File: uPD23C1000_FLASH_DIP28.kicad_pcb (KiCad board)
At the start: 2 copper layers, 16.4 x 34.2 mm, 7 parts, among them J1 uPD23C1000, J2 Conn_1x2, J3 Conn_1x3, U1 GLS29EE010 (TSOP), U2 SST39SF010 (TSOP), U3 SST39SF010 / GLS29EE010 (PLCC)

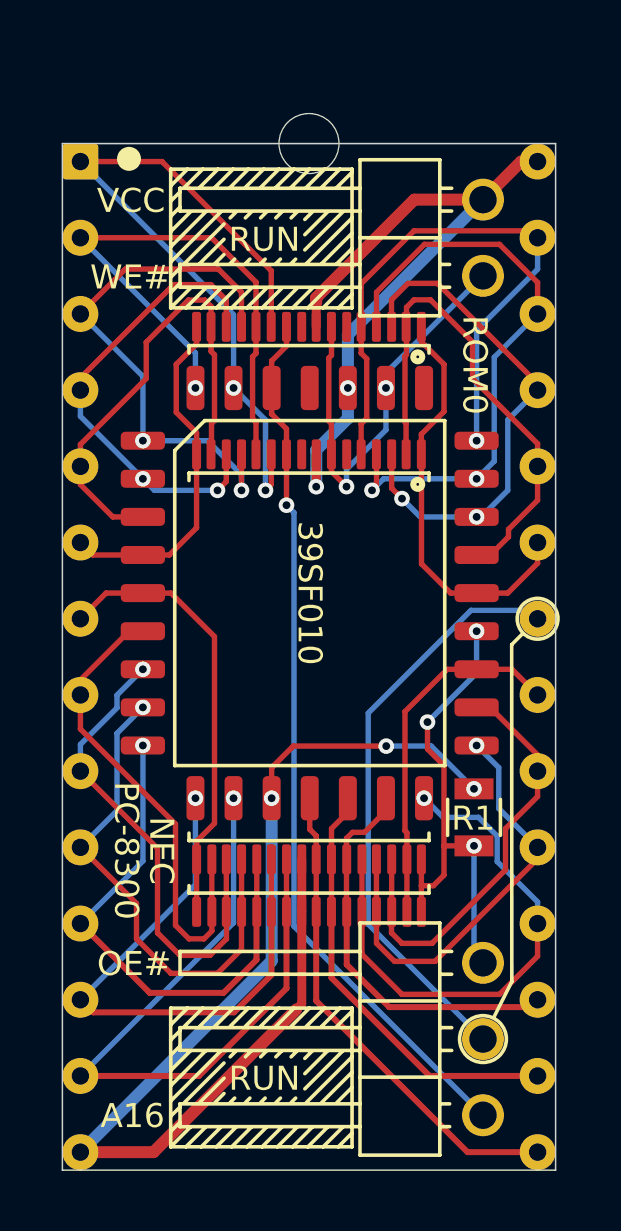
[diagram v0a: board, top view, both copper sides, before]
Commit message: FlashROM_8300: tsop footprints, zone fills
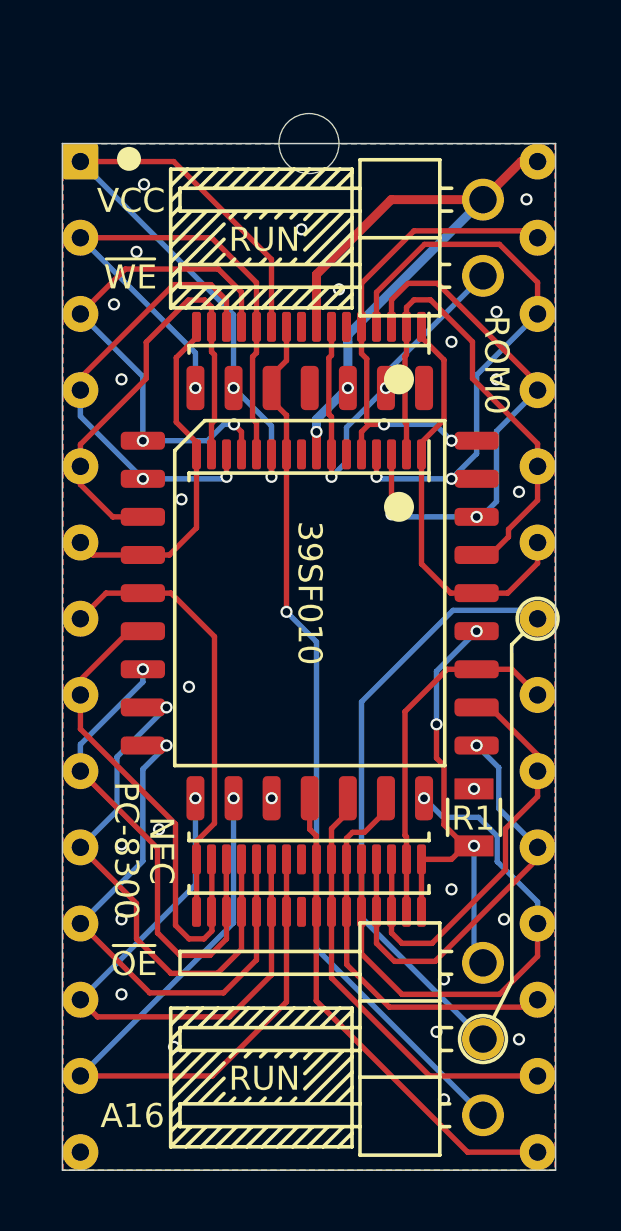
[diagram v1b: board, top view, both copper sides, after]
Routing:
- net /GND: track 37.3 -> 0.00 mm, vias 3 -> 26
- net /A14: track 20.2 -> 16.4 mm, vias 1 -> 2
- net /VCC: track 23.2 -> 21.5 mm
- net /A7: track 18.1 -> 16.8 mm
- net /D0: track 17.4 -> 18.5 mm
- net /A0: track 16.7 -> 17.8 mm
- net /~OE: track 16.7 -> 15.8 mm
- net /A15: track 24.5 -> 23.9 mm
- net /~WE: track 14.5 -> 13.9 mm
- net /A16_OE: track 19.6 -> 20.2 mm
- net /A8: track 17.1 -> 17.6 mm
- added copper zone on B.Cu, net /GND
- added copper zone on F.Cu, net /GND
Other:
- net class Default: clearance 0.2 -> 0.1524; trace_width 0.25 -> 0.18; via_dia 0.8 -> 0.4064; via_drill 0.4 -> 0.254
- rule trace_clearance: 0.2 -> 0.1524
- rule trace_min: 0.16 -> 0.1524
- rule via_min_drill: 0.26 -> 0.254
- rule via_min_size: 0.52 -> 0.4064
- board text added: "Connect ~WE~ to programmer pin 31"
- board text added: "Move A16 jumper to ~OE~"
- board text added: "Remove VCC/~WE~ jumper"
- board text added: "~OE"
- board text added: "~WE"
- board text removed: "Connect WE# to programmer pin 31"
- board text removed: "Move A16 jumper to OE#"
- board text removed: "OE#"
- board text removed: "Remove VCC/WE# jumper"
- board text removed: "WE#"

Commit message: minor tidying
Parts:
- moved J2 1.89 mm to (155.7, 85.4)
- moved U1 1.30 mm to (150.0, 97.5)
- moved J1 1.25 mm to (150.0, 98.8)
- moved J3 0.66 mm to (155.7, 114.6)
- moved R1 0.60 mm to (155.4, 106.0)
- moved U2 0.45 mm to (150.0, 100.5)
- moved U3 0.42 mm to (150.0, 97.5)
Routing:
- net /GND: track 0.00 -> 24.4 mm, vias 26 -> 2
- net /A15: track 23.9 -> 17.1 mm, vias 2 -> 0
- net /D6: track 17.8 -> 11.2 mm, vias 1 -> 2
- net /A14: track 16.4 -> 22.3 mm, vias 2 -> 1
- net /A16_OE: track 20.2 -> 15.4 mm
- net /VCC: track 21.5 -> 17.4 mm, vias 2 -> 0
- net /~CE: track 14.4 -> 10.4 mm
- net /~WE: track 13.9 -> 16.8 mm, vias 2 -> 3
- net /D0: track 18.5 -> 15.7 mm
- net /A0: track 17.8 -> 15.0 mm
- net /D7: track 14.5 -> 11.8 mm, vias 1 -> 0
- net /A12: track 18.8 -> 16.3 mm, vias 1 -> 3
- net /~OE: track 15.8 -> 13.3 mm, vias 3 -> 2
- net /D2: track 24.0 -> 21.6 mm
- net /A16: track 29.4 -> 31.6 mm
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- removed copper zone on B.Cu, net /GND
- removed copper zone on F.Cu, net /GND
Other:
- board size 16.4 x 34.2 mm -> 16.6 x 34.4 mm
- board text added: "29F010 39SF010 29EE010"
- board text added: "29F010 to uPD23C1000"
- board text added: "Move the A16 jumper to ~OE~"
- board text added: "Remove the VCC/~WE~ jumper"
- board text added: "Set programmer for installed chip (ex: SST39SF010 not uPD23C1000)"
- board text added: "github.com/bkw777/aDIPters"
- board text removed: "39SF010"
- board text removed: "Configure programmer for PLCC version of chip (even if chip is TSOP)"
- board text removed: "Move A16 jumper to ~OE~"
- board text removed: "NEC"
- board text removed: "NEC PC-8300 System ROM"
- board text removed: "PC-8300"
- board text removed: "ROM0"
- board text removed: "Remove VCC/~WE~ jumper"
- board text removed: "http://tandy.wiki/FlashROM_8300"

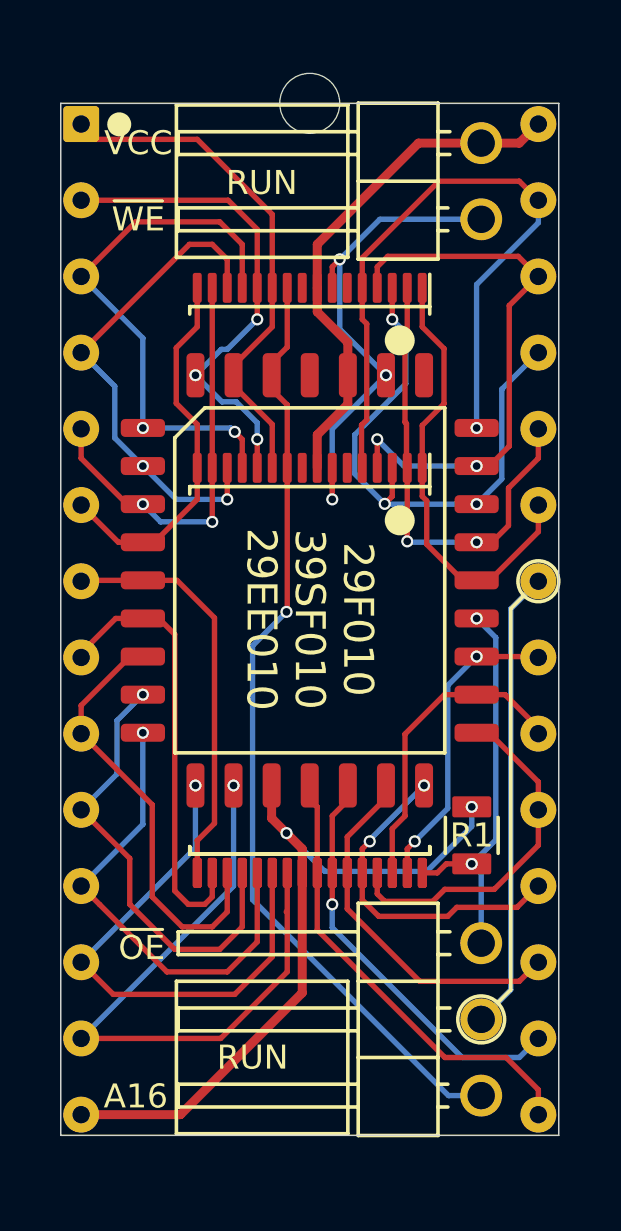
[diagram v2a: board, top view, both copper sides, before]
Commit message: upD23C1000 add A17 & R2
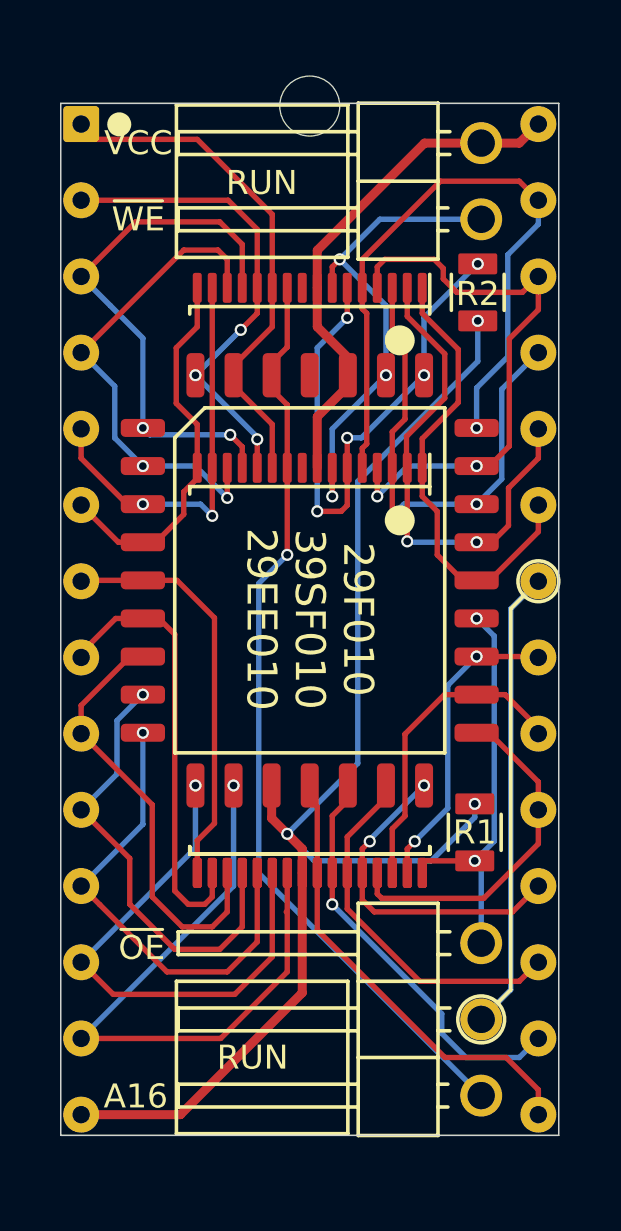
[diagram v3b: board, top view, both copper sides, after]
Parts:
- added R2: 47k, 000_LOCAL:R_0805, F.Cu at (155.6, 87.8)
- J1: footprint 000_LOCAL:DIP-28_W15.24mm_pcb_sil_pins -> 000_LOCAL:DIP28_0.6_pcb_sil_pins
- J2: footprint 000_LOCAL:Pin_Header_Angled_1x02_Pitch2.54mm -> 000_LOCAL:Pin_Header_Angled_1x02_Pitch2.54mm_shorted
- J3: footprint 000_LOCAL:Pin_Header_Angled_1x03_Pitch2.54mm -> 000_LOCAL:Pin_Header_Angled_1x03_Pitch2.54mm_12shorted
- U1: value GLS29EE010 (TSOP) -> 29F0x0 (TSOP)
- U2: value SST39SF010 (TSOP) -> 29F0x0 (TSOP)
- U3: value SST39SF010 / GLS29EE010 (PLCC) -> 29F0x0 (PLCC)
- moved R1 0.14 mm to (155.5, 105.8)
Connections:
- U1 pad 6: (no net) -> /A17
- U2 pad 6: (no net) -> /A17
- U3 pad 30: (no net) -> /A17
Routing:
- net /GND: track 24.4 -> 43.8 mm, vias 2 -> 3
- net /A17: track 0.00 -> 19.1 mm, vias 0 -> 5
- net /A8: track 18.8 -> 16.8 mm, vias 3 -> 2
- net /A9: track 15.3 -> 16.3 mm
- net /A16: track 31.6 -> 30.8 mm
- net /A13: track 18.6 -> 19.2 mm

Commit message: uPD23C1000 & FlashROM_8300 correct A17 & A18 handling
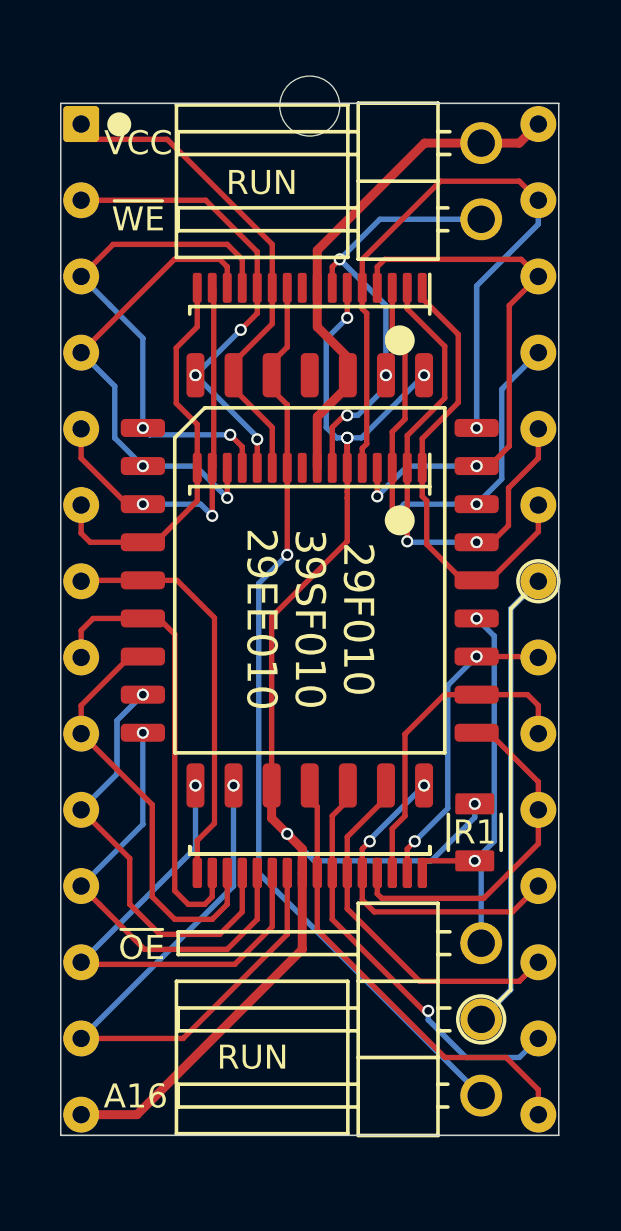
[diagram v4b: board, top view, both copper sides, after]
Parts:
- removed R2: 47k, 000_LOCAL:R_0805
- added NT1: Net-Tie_2, 000_LOCAL:NetTie-2_SMD_0.18mm, F.Cu at (151.3, 94.6)
- U1: value 29F0x0 (TSOP) -> 29F010 TSOP-32 20mm
- U2: value 29F0x0 (TSOP) -> 29F010 sTSOP-32 14mm
- U3: value 29F0x0 (PLCC) -> 29F010 PLCC-32 7x9
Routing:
- net /GND: track 43.8 -> 33.8 mm, vias 3 -> 2
- net /A17: track 19.1 -> 12.0 mm, vias 5 -> 4
- net /~WE: track 16.6 -> 14.9 mm
- net /D1: track 17.6 -> 16.2 mm
- net /D0: track 15.7 -> 14.7 mm
- net /A7: track 18.1 -> 17.1 mm
- net /D2: track 21.6 -> 20.9 mm
- net /A0: track 15.0 -> 14.3 mm
- net /A13: track 19.2 -> 18.6 mm
- net /A15: track 17.1 -> 16.5 mm
- net /A4: track 12.6 -> 13.2 mm

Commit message: minor touches
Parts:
- added REF**: NPTH_3mm, 000_LOCAL:NPTH_3mm, F.Cu at (150.0, 81.6)
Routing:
- net /A0: track 14.3 -> 13.7 mm
- net /GND: track 33.8 -> 33.3 mm
- net /A17: track 12.0 -> 11.8 mm, vias 4 -> 3
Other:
- board size 16.6 x 34.4 mm -> 16.5 x 34.3 mm
